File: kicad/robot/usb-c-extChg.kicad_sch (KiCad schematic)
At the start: 11 parts, among them J1 USBC_Receptacle_SMD_RA

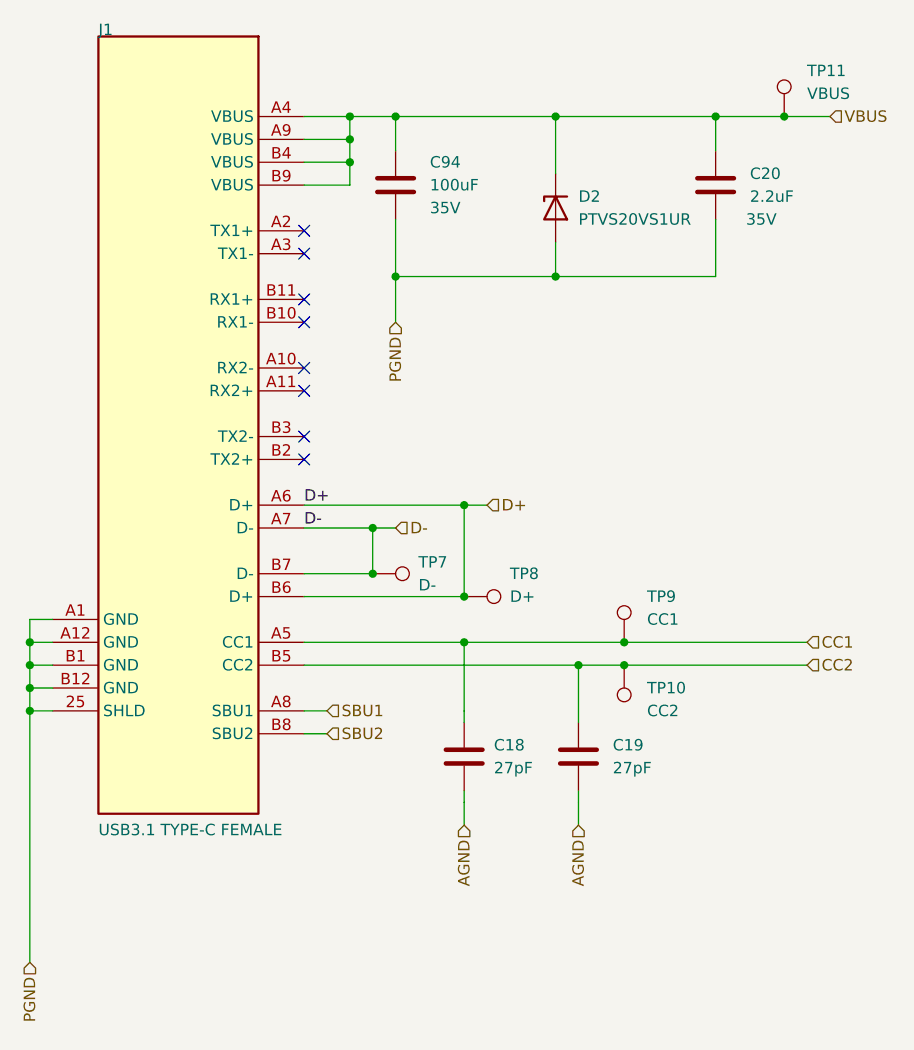
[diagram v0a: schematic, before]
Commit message: Renamed USB sheets
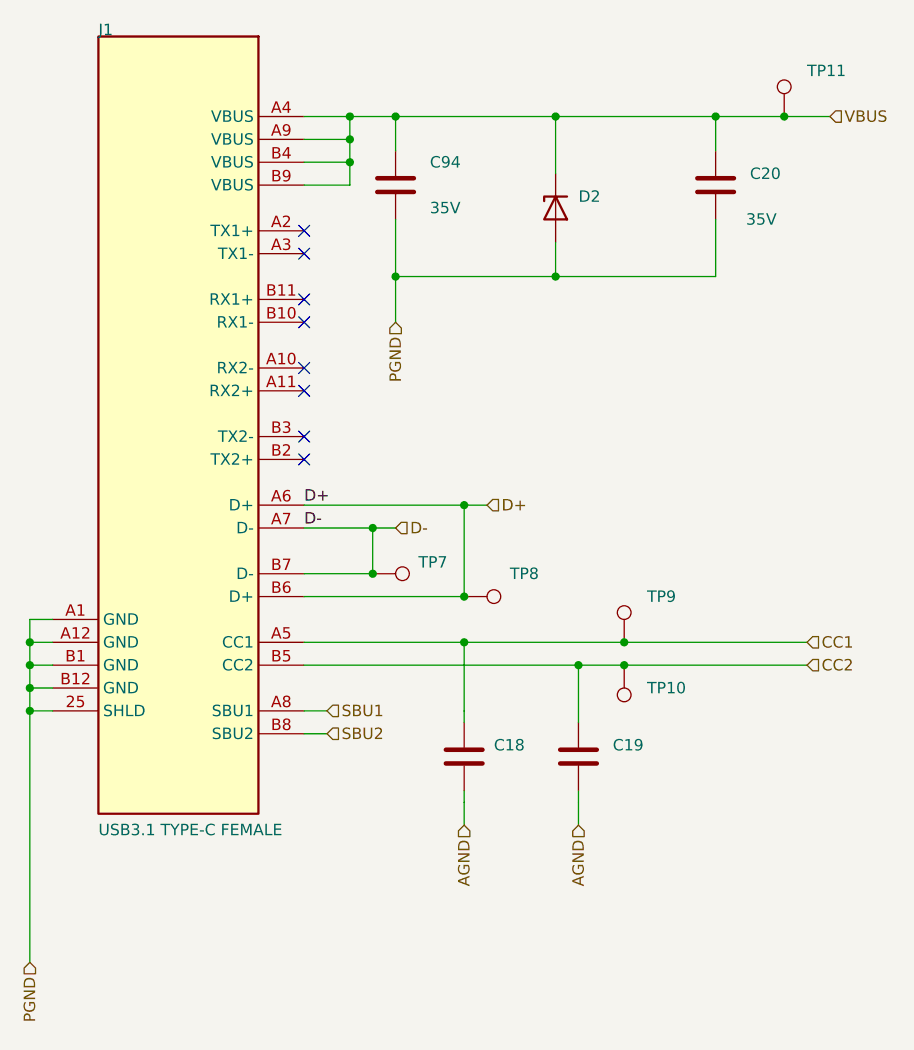
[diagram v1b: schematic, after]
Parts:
- C18, C19: value 27pF -> (none); footprint Capacitor_SMD:C_0402_1005Metric -> (none)
- C20: value 2.2uF -> (none); footprint Capacitor_SMD:C_0805_2012Metric -> (none)
- C94: value 100uF -> (none); footprint Capacitor_SMD:C_1210_3225Metric -> (none)
- D2: value PTVS20VS1UR -> (none); footprint Diode_SMD:Nexperia_CFP3_SOD-123W -> (none)
- J1: value USBC_Receptacle_SMD_RA -> (none); footprint AltiumImports:CON_USB3.1-C_RCPT_SMD_RA_ACP_12401610E4#2A -> (none)
- TP10: value CC2 -> (none); footprint TestPoint:KEYSTONE_5002 -> (none)
- TP11: value VBUS -> (none); footprint TestPoint:KEYSTONE_5002 -> (none)
- TP7: value D- -> (none); footprint TestPoint:KEYSTONE_5002 -> (none)
- TP8: value D+ -> (none); footprint TestPoint:KEYSTONE_5002 -> (none)
- TP9: value CC1 -> (none); footprint TestPoint:KEYSTONE_5002 -> (none)
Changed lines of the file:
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@@
       (effects (font (size 1.27 1.27)) (justify left))
     )
-    (property "Value" "2.2uF" (id 1) (at 189.23 80.0099 0)
-      (effects (font (size 1.27 1.27)) (justify left))
-    )
-    (property "Footprint" "Capacitor_SMD:C_0805_2012Metric" (id 2) (at 186.3852 82.55 0)
+    (property "Value" "" (id 1) (at 189.23 80.0099 0)
+      (effects (font (size 1.27 1.27)) (justify left))
+    )
+    (property "Footprint" "" (id 2) (at 186.3852 82.55 0)
       (effects (font (size 1.27 1.27)) hide)
     )
@@
       (effects (font (size 1.27 1.27)) (justify left))
     )
-    (property "Value" "D+" (id 1) (at 162.56 124.46 90)
-      (effects (font (size 1.27 1.27)) (justify left))
-    )
-    (property "Footprint" "TestPoint:KEYSTONE_5002" (id 2) (at 157.48 129.54 0)
+    (property "Value" "" (id 1) (at 162.56 124.46 90)
+      (effects (font (size 1.27 1.27)) (justify left))
+    )
+    (property "Footprint" "" (id 2) (at 157.48 129.54 0)
       (effects (font (size 1.27 1.27)) hide)
     )
@@
       (effects (font (size 1.27 1.27)) (justify right))
     )
-    (property "Value" "PTVS20VS1UR" (id 1) (at 170.18 82.5499 90)
-      (effects (font (size 1.27 1.27)) (justify right))
-    )
-    (property "Footprint" "Diode_SMD:Nexperia_CFP3_SOD-123W" (id 2) (at 167.64 81.28 0)
+    (property "Value" "" (id 1) (at 170.18 82.5499 90)
+      (effects (font (size 1.27 1.27)) (justify right))
+    )
+    (property "Footprint" "" (id 2) (at 167.64 81.28 0)
       (effects (font (size 1.27 1.27)) hide)
     )
@@
       (effects (font (size 1.27 1.27)) (justify left))
     )
-    (property "Value" "100uF" (id 1) (at 153.67 78.7399 0)
-      (effects (font (size 1.27 1.27)) (justify left))
-    )
-    (property "Footprint" "Capacitor_SMD:C_1210_3225Metric" (id 2) (at 150.8252 82.55 0)
+    (property "Value" "" (id 1) (at 153.67 78.7399 0)
+      (effects (font (size 1.27 1.27)) (justify left))
+    )
+    (property "Footprint" "" (id 2) (at 150.8252 82.55 0)
       (effects (font (size 1.27 1.27)) hide)
     )
@@
       (effects (font (size 1.27 1.27)) (justify left))
     )
-    (property "Value" "CC1" (id 1) (at 177.8 127 0)
-      (effects (font (size 1.27 1.27)) (justify left))
-    )
-    (property "Footprint" "TestPoint:KEYSTONE_5002" (id 2) (at 180.34 129.54 0)
+    (property "Value" "" (id 1) (at 177.8 127 0)
+      (effects (font (size 1.27 1.27)) (justify left))
+    )
+    (property "Footprint" "" (id 2) (at 180.34 129.54 0)
       (effects (font (size 1.27 1.27)) hide)
     )
@@
       (effects (font (size 1.27 1.27)) (justify left))
     )
-    (property "Value" "27pF" (id 1) (at 173.99 143.5099 0)
-      (effects (font (size 1.27 1.27)) (justify left))
-    )
-    (property "Footprint" "Capacitor_SMD:C_0402_1005Metric" (id 2) (at 171.1452 146.05 0)
+    (property "Value" "" (id 1) (at 173.99 143.5099 0)
+      (effects (font (size 1.27 1.27)) (justify left))
+    )
+    (property "Footprint" "" (id 2) (at 171.1452 146.05 0)
       (effects (font (size 1.27 1.27)) hide)
     )
@@
       (effects (font (size 1.27 1.27)) (justify left))
     )
-    (property "Value" "VBUS" (id 1) (at 195.58 68.58 0)
-      (effects (font (size 1.27 1.27)) (justify left))
-    )
-    (property "Footprint" "TestPoint:KEYSTONE_5002" (id 2) (at 198.12 71.12 0)
+    (property "Value" "" (id 1) (at 195.58 68.58 0)
+      (effects (font (size 1.27 1.27)) (justify left))
+    )
+    (property "Footprint" "" (id 2) (at 198.12 71.12 0)
       (effects (font (size 1.27 1.27)) hide)
     )
@@
       (effects (font (size 1.27 1.27)) (justify left bottom))
     )
-    (property "Value" "USBC_Receptacle_SMD_RA" (id 1) (at 111.252 62.23 0)
-      (effects (font (size 1.27 1.27)) (justify left bottom) hide)
-    )
-    (property "Footprint" "AltiumImports:CON_USB3.1-C_RCPT_SMD_RA_ACP_12401610E4#2A" (id 2) (at 134.62 62.23 0)
+    (property "Value" "" (id 1) (at 111.252 62.23 0)
+      (effects (font (size 1.27 1.27)) (justify left bottom) hide)
+    )
+    (property "Footprint" "" (id 2) (at 134.62 62.23 0)
       (effects (font (size 1.27 1.27)) hide)
     )
@@
       (effects (font (size 1.27 1.27)) (justify left))
     )
-    (property "Value" "D-" (id 1) (at 152.4 123.1899 90)
-      (effects (font (size 1.27 1.27)) (justify left))
-    )
-    (property "Footprint" "TestPoint:KEYSTONE_5002" (id 2) (at 147.32 127 0)
+    (property "Value" "" (id 1) (at 152.4 123.1899 90)
+      (effects (font (size 1.27 1.27)) (justify left))
+    )
+    (property "Footprint" "" (id 2) (at 147.32 127 0)
       (effects (font (size 1.27 1.27)) hide)
     )
@@
       (effects (font (size 1.27 1.27)) (justify right))
     )
-    (property "Value" "CC2" (id 1) (at 177.8 137.16 0)
-      (effects (font (size 1.27 1.27)) (justify right))
-    )
-    (property "Footprint" "TestPoint:KEYSTONE_5002" (id 2) (at 170.18 132.08 0)
+    (property "Value" "" (id 1) (at 177.8 137.16 0)
+      (effects (font (size 1.27 1.27)) (justify right))
+    )
+    (property "Footprint" "" (id 2) (at 170.18 132.08 0)
       (effects (font (size 1.27 1.27)) hide)
     )
@@
       (effects (font (size 1.27 1.27)) (justify left))
     )
-    (property "Value" "27pF" (id 1) (at 160.782 143.51 0)
-      (effects (font (size 1.27 1.27)) (justify left))
-    )
-    (property "Footprint" "Capacitor_SMD:C_0402_1005Metric" (id 2) (at 158.4452 146.05 0)
-      (effects (font (size 1.27 1.27)) hide)
-    )
+    (property "Value" "" (id 1) (at 160.782 143.51 0)
+      (effects (font (size 1.27 1.27)) (justify left))
+    )
+    (property "Footprint" "" (id 2) (at 158.4452 146.05 0)
+      (effects (font (size 1.27 1.27)) hide)
+    )

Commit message: MAJOR REVISION. MAX77958 moved to new sheet and 2nd USB connector added
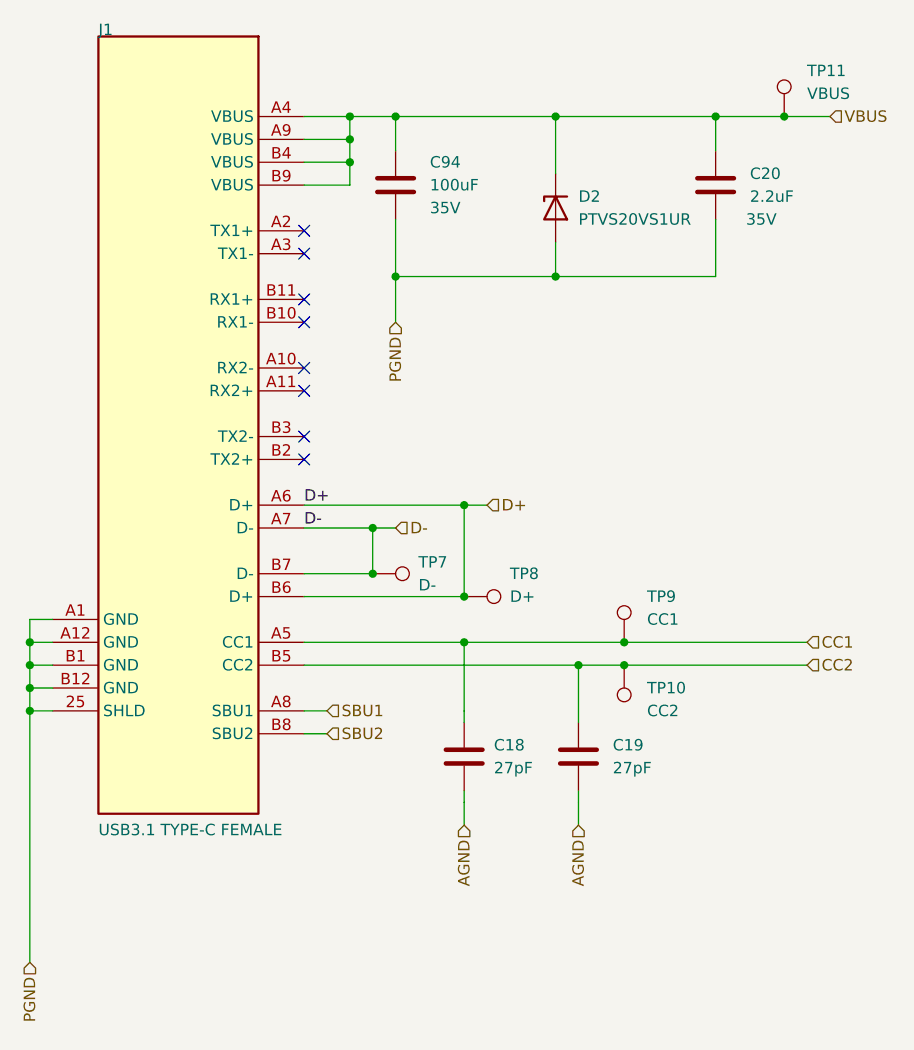
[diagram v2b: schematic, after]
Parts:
- C18, C19: value (none) -> 27pF; footprint (none) -> Capacitor_SMD:C_0402_1005Metric
- C20: value (none) -> 2.2uF; footprint (none) -> Capacitor_SMD:C_0805_2012Metric
- C94: value (none) -> 100uF; footprint (none) -> Capacitor_SMD:C_1210_3225Metric
- D2: value (none) -> PTVS20VS1UR; footprint (none) -> Diode_SMD:Nexperia_CFP3_SOD-123W
- J1: value (none) -> USBC_Receptacle_SMD_RA; footprint (none) -> AltiumImports:CON_USB3.1-C_RCPT_SMD_RA_ACP_12401610E4#2A
- TP10: value (none) -> CC2; footprint (none) -> TestPoint:KEYSTONE_5002
- TP11: value (none) -> VBUS; footprint (none) -> TestPoint:KEYSTONE_5002
- TP7: value (none) -> D-; footprint (none) -> TestPoint:KEYSTONE_5002
- TP8: value (none) -> D+; footprint (none) -> TestPoint:KEYSTONE_5002
- TP9: value (none) -> CC1; footprint (none) -> TestPoint:KEYSTONE_5002
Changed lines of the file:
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@@
       (effects (font (size 1.27 1.27)) (justify left))
     )
-    (property "Value" "" (id 1) (at 189.23 80.0099 0)
-      (effects (font (size 1.27 1.27)) (justify left))
-    )
-    (property "Footprint" "" (id 2) (at 186.3852 82.55 0)
+    (property "Value" "2.2uF" (id 1) (at 189.23 80.0099 0)
+      (effects (font (size 1.27 1.27)) (justify left))
+    )
+    (property "Footprint" "Capacitor_SMD:C_0805_2012Metric" (id 2) (at 186.3852 82.55 0)
       (effects (font (size 1.27 1.27)) hide)
     )
@@
       (effects (font (size 1.27 1.27)) (justify left))
     )
-    (property "Value" "" (id 1) (at 162.56 124.46 90)
-      (effects (font (size 1.27 1.27)) (justify left))
-    )
-    (property "Footprint" "" (id 2) (at 157.48 129.54 0)
+    (property "Value" "D+" (id 1) (at 162.56 124.46 90)
+      (effects (font (size 1.27 1.27)) (justify left))
+    )
+    (property "Footprint" "TestPoint:KEYSTONE_5002" (id 2) (at 157.48 129.54 0)
       (effects (font (size 1.27 1.27)) hide)
     )
@@
       (effects (font (size 1.27 1.27)) (justify right))
     )
-    (property "Value" "" (id 1) (at 170.18 82.5499 90)
-      (effects (font (size 1.27 1.27)) (justify right))
-    )
-    (property "Footprint" "" (id 2) (at 167.64 81.28 0)
+    (property "Value" "PTVS20VS1UR" (id 1) (at 170.18 82.5499 90)
+      (effects (font (size 1.27 1.27)) (justify right))
+    )
+    (property "Footprint" "Diode_SMD:Nexperia_CFP3_SOD-123W" (id 2) (at 167.64 81.28 0)
       (effects (font (size 1.27 1.27)) hide)
     )
@@
       (effects (font (size 1.27 1.27)) (justify left))
     )
-    (property "Value" "" (id 1) (at 153.67 78.7399 0)
-      (effects (font (size 1.27 1.27)) (justify left))
-    )
-    (property "Footprint" "" (id 2) (at 150.8252 82.55 0)
+    (property "Value" "100uF" (id 1) (at 153.67 78.7399 0)
+      (effects (font (size 1.27 1.27)) (justify left))
+    )
+    (property "Footprint" "Capacitor_SMD:C_1210_3225Metric" (id 2) (at 150.8252 82.55 0)
       (effects (font (size 1.27 1.27)) hide)
     )
@@
       (effects (font (size 1.27 1.27)) (justify left))
     )
-    (property "Value" "" (id 1) (at 177.8 127 0)
-      (effects (font (size 1.27 1.27)) (justify left))
-    )
-    (property "Footprint" "" (id 2) (at 180.34 129.54 0)
+    (property "Value" "CC1" (id 1) (at 177.8 127 0)
+      (effects (font (size 1.27 1.27)) (justify left))
+    )
+    (property "Footprint" "TestPoint:KEYSTONE_5002" (id 2) (at 180.34 129.54 0)
       (effects (font (size 1.27 1.27)) hide)
     )
@@
       (effects (font (size 1.27 1.27)) (justify left))
     )
-    (property "Value" "" (id 1) (at 173.99 143.5099 0)
-      (effects (font (size 1.27 1.27)) (justify left))
-    )
-    (property "Footprint" "" (id 2) (at 171.1452 146.05 0)
+    (property "Value" "27pF" (id 1) (at 173.99 143.5099 0)
+      (effects (font (size 1.27 1.27)) (justify left))
+    )
+    (property "Footprint" "Capacitor_SMD:C_0402_1005Metric" (id 2) (at 171.1452 146.05 0)
       (effects (font (size 1.27 1.27)) hide)
     )
@@
       (effects (font (size 1.27 1.27)) (justify left))
     )
-    (property "Value" "" (id 1) (at 195.58 68.58 0)
-      (effects (font (size 1.27 1.27)) (justify left))
-    )
-    (property "Footprint" "" (id 2) (at 198.12 71.12 0)
+    (property "Value" "VBUS" (id 1) (at 195.58 68.58 0)
+      (effects (font (size 1.27 1.27)) (justify left))
+    )
+    (property "Footprint" "TestPoint:KEYSTONE_5002" (id 2) (at 198.12 71.12 0)
       (effects (font (size 1.27 1.27)) hide)
     )
@@
       (effects (font (size 1.27 1.27)) (justify left bottom))
     )
-    (property "Value" "" (id 1) (at 111.252 62.23 0)
-      (effects (font (size 1.27 1.27)) (justify left bottom) hide)
-    )
-    (property "Footprint" "" (id 2) (at 134.62 62.23 0)
+    (property "Value" "USBC_Receptacle_SMD_RA" (id 1) (at 111.252 62.23 0)
+      (effects (font (size 1.27 1.27)) (justify left bottom) hide)
+    )
+    (property "Footprint" "AltiumImports:CON_USB3.1-C_RCPT_SMD_RA_ACP_12401610E4#2A" (id 2) (at 134.62 62.23 0)
       (effects (font (size 1.27 1.27)) hide)
     )
@@
       (effects (font (size 1.27 1.27)) (justify left))
     )
-    (property "Value" "" (id 1) (at 152.4 123.1899 90)
-      (effects (font (size 1.27 1.27)) (justify left))
-    )
-    (property "Footprint" "" (id 2) (at 147.32 127 0)
+    (property "Value" "D-" (id 1) (at 152.4 123.1899 90)
+      (effects (font (size 1.27 1.27)) (justify left))
+    )
+    (property "Footprint" "TestPoint:KEYSTONE_5002" (id 2) (at 147.32 127 0)
       (effects (font (size 1.27 1.27)) hide)
     )
@@
       (effects (font (size 1.27 1.27)) (justify right))
     )
-    (property "Value" "" (id 1) (at 177.8 137.16 0)
-      (effects (font (size 1.27 1.27)) (justify right))
-    )
-    (property "Footprint" "" (id 2) (at 170.18 132.08 0)
+    (property "Value" "CC2" (id 1) (at 177.8 137.16 0)
+      (effects (font (size 1.27 1.27)) (justify right))
+    )
+    (property "Footprint" "TestPoint:KEYSTONE_5002" (id 2) (at 170.18 132.08 0)
       (effects (font (size 1.27 1.27)) hide)
     )
@@
       (effects (font (size 1.27 1.27)) (justify left))
     )
-    (property "Value" "" (id 1) (at 160.782 143.51 0)
-      (effects (font (size 1.27 1.27)) (justify left))
-    )
-    (property "Footprint" "" (id 2) (at 158.4452 146.05 0)
-      (effects (font (size 1.27 1.27)) hide)
-    )
+    (property "Value" "27pF" (id 1) (at 160.782 143.51 0)
+      (effects (font (size 1.27 1.27)) (justify left))
+    )
+    (property "Footprint" "Capacitor_SMD:C_0402_1005Metric" (id 2) (at 158.4452 146.05 0)
+      (effects (font (size 1.27 1.27)) hide)
+    )

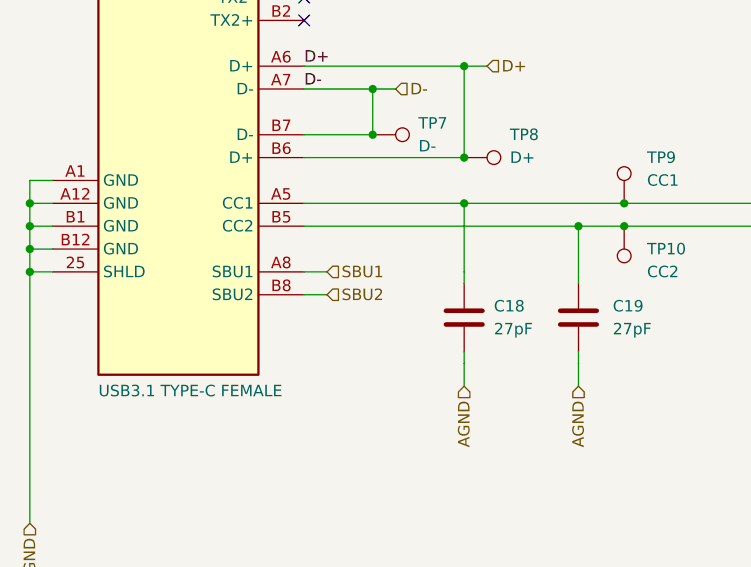
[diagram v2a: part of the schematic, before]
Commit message: MAJOR REVISON. Added USB-PD-ExtChg sheet contents
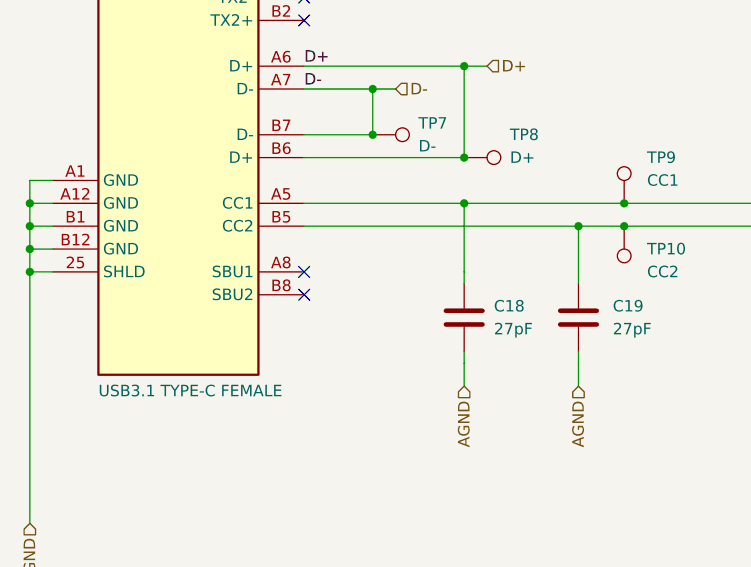
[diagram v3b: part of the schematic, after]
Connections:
- net SBU1: no longer names the net of J1.A8 (SBU1)
- net SBU2: no longer names the net of J1.B8 (SBU2)
- no-connect marks 8 -> 10
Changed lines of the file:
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@@
   (no_connect (at 139.7 91.44))
   (no_connect (at 139.7 83.82))
+  (no_connect (at 139.7 137.16))
+  (no_connect (at 139.7 139.7))
   (no_connect (at 139.7 86.36))
   (no_connect (at 139.7 106.68))
@@
     (stroke (width 0.254) (type default) (color 0 0 0 0))
   )
-  (wire (pts (xy 139.7 139.7) (xy 142.24 139.7))
-    (stroke (width 0) (type default) (color 0 0 0 0))
-  )
   (wire (pts (xy 139.7 73.66) (xy 144.78 73.66))
     (stroke (width 0.254) (type default) (color 0 0 0 0))
@@
   (wire (pts (xy 147.32 121.92) (xy 147.32 116.84))
     (stroke (width 0.254) (type default) (color 0 0 0 0))
-  )
-  (wire (pts (xy 139.7 137.16) (xy 142.24 137.16))
-    (stroke (width 0) (type default) (color 0 0 0 0))
   )
   (wire (pts (xy 157.48 129.54) (xy 175.26 129.54))
@@
     (effects (font (size 1.27 1.27)) (justify left))
   )
-  (hierarchical_label "SBU2" (shape input) (at 142.24 139.7 0)
-    (effects (font (size 1.27 1.27)) (justify left))
-  )
   (hierarchical_label "D-" (shape input) (at 149.86 116.84 0)
     (effects (font (size 1.27 1.27)) (justify left))
@@
     (effects (font (size 1.27 1.27)) (justify left))
   )
-  (hierarchical_label "SBU1" (shape input) (at 142.24 137.16 0)
-    (effects (font (size 1.27 1.27)) (justify left))
-  )
